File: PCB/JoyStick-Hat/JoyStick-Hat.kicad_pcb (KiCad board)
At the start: 4 copper layers, 65 x 120 mm, 109 parts, among them J1 20021121-00010C4LF, J10 Conn_02x06_Odd_Even, J14 Conn_01x03_Pin, J15 Conn_01x03_Pin, J2 BU2032SM-JJ-GTR, J3 Conn_02x05_Odd_Even, J4 Conn_02x04_Odd_Even, J5 8P8C_LED_Shielded, J6 1757242, J7 Raspberry_Pi_2_3, J8 Conn_02x04_Odd_Even, J9 1755736, M1 D24V22F12, M2 D24V22F5, M3 D24V22F3, SW1 TL3301NF260QG, U1 STM32F446VETx, U4 MAX3535ECWI+T, X1 ABM3B-8.000MHZ-B2-T, X2 ABS07-32.768KHZ-9-T

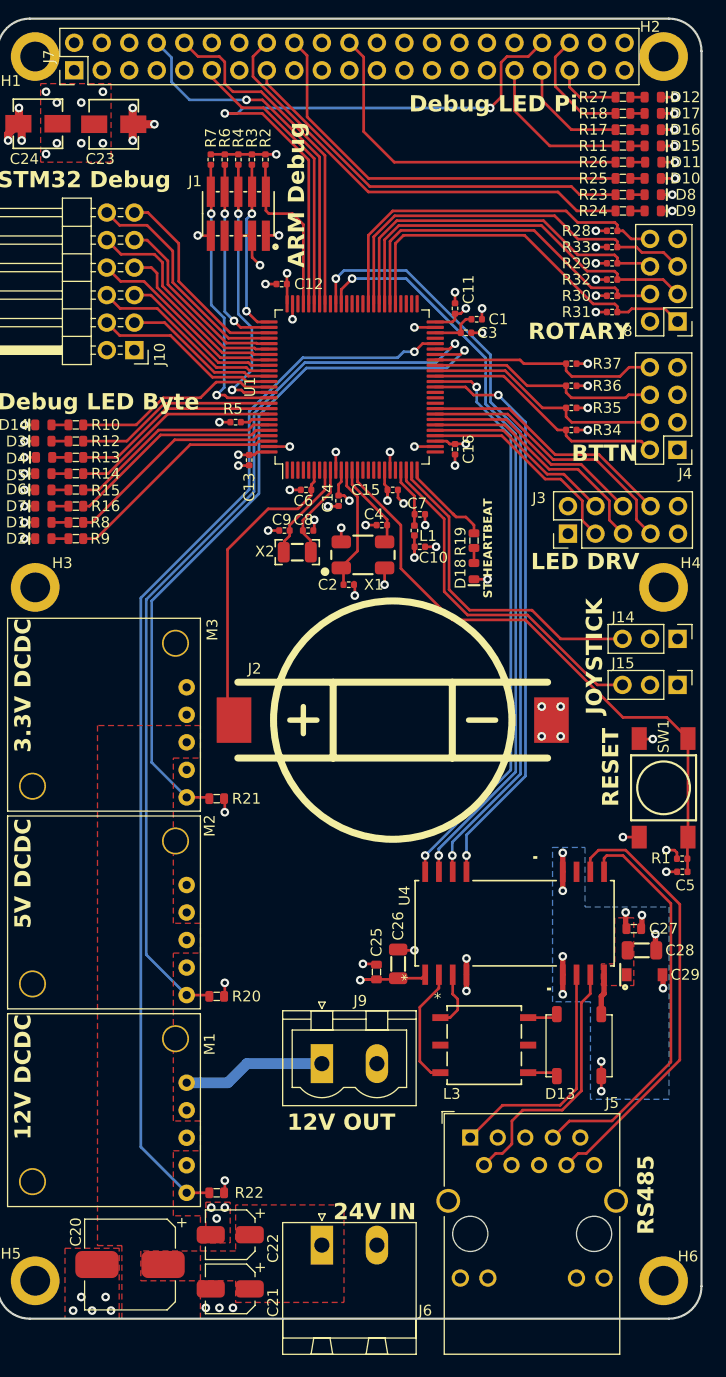
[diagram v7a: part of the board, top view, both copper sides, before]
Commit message: James Fixes and 3D models
Added all the changes that James suggested to the design and then added 3D models to the board for mechanical design purposes. Generated 3D renders of the board and added them to new directory called img.
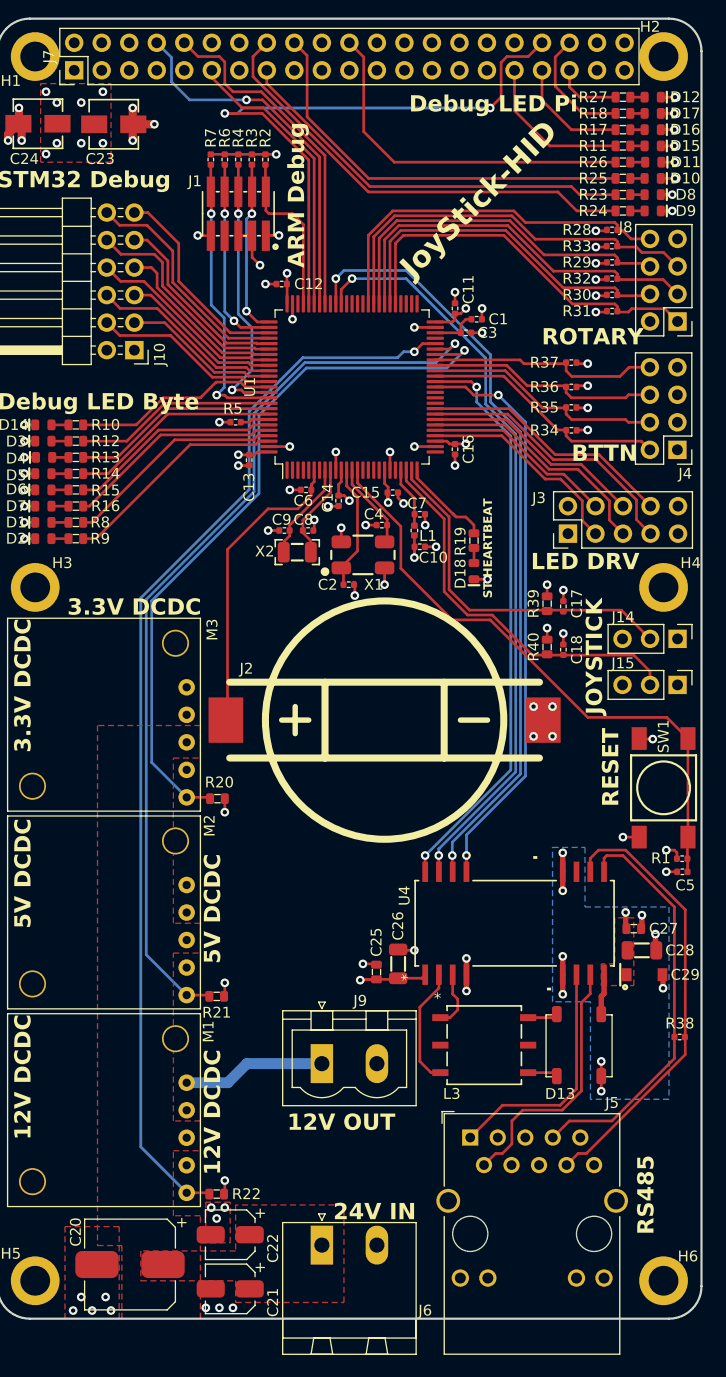
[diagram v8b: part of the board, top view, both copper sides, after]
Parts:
- added C17: C0402C104K9PACTU, AVR-KiCAD-Lib-Resistors:R0402, F.Cu at (252.2, 93.8)
- added C18: C0402C104K9PACTU, AVR-KiCAD-Lib-Resistors:R0402, F.Cu at (252.2, 97.8)
- added R38: AC0402FR-07120RL, AVR-KiCAD-Lib-Resistors:R0402, F.Cu at (263.0, 133.5)
- added R39: RT0603BRD071ML, AVR-KiCAD-Lib-Resistors:R0603, F.Cu at (250.8, 93.5)
- added R40: RT0603BRD071ML, AVR-KiCAD-Lib-Resistors:R0603, F.Cu at (250.8, 97.5)
- R20, R21, R22: value RC0603JR-07270RL -> RC0603FR-072K2L
- R28, R29, R30, R31, R32, R33, R34, R35, R36, R37: value RC0402FR-071KL -> RC0402FR-072K2L
- moved R20 18.3 mm to (220.3, 111.5)
- moved R21 18.2 mm to (220.2, 129.8)
- moved J2 0.75 mm to (235.8, 104.2)
- moved C15 0.25 mm to (236.5, 83.2)
- moved R22 0.12 mm to (220.2, 148.0)
- moved R36 0.11 mm to (253.0, 73.5), turned to 0 degrees
- moved R37 0.10 mm to (253.0, 71.2), turned to 0 degrees
- moved R33 0.09 mm to (256.7, 60.5), turned to 180 degrees
- moved R28 0.09 mm to (256.8, 59.0), turned to 180 degrees
- moved R29 0.09 mm to (256.8, 62.0), turned to 180 degrees
- moved R32 0.09 mm to (256.8, 63.5), turned to 180 degrees
- moved R30 0.08 mm to (256.8, 65.0), turned to 180 degrees
- moved R31 0.08 mm to (256.8, 66.5), turned to 180 degrees
- turned R35 to 0 degrees
- turned R34 to 0 degrees
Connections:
- J14 pad 2: +3.3V -> /JoyStick Interface/JOYSTICK_X
- J14 pad 3: /JoyStick Interface/JOYSTICK_X -> +3.3V
- J15 pad 2: +3.3V -> /JoyStick Interface/JOYSTICK_Y
- J15 pad 3: /JoyStick Interface/JOYSTICK_Y -> +3.3V
- R20 pad 1: /Power/5V_PG -> /Power/3.3V_PG
- R21 pad 1: /Power/3.3V_PG -> /Power/5V_PG
- R28 pad 1: +3.3V -> /JoyStick Interface/ROTARY2_POLE1
- R28 pad 2: /JoyStick Interface/ROTARY2_POLE1 -> +3.3V
- R29 pad 1: +3.3V -> /JoyStick Interface/ROTARY2_POLE2
- R29 pad 2: /JoyStick Interface/ROTARY2_POLE2 -> +3.3V
- R30 pad 1: +3.3V -> /JoyStick Interface/ROTARY2_POLE3
- R30 pad 2: /JoyStick Interface/ROTARY2_POLE3 -> +3.3V
- R31 pad 1: +3.3V -> /JoyStick Interface/ROTARY1_POLE1
- R31 pad 2: /JoyStick Interface/ROTARY1_POLE1 -> +3.3V
- R32 pad 1: +3.3V -> /JoyStick Interface/ROTARY1_POLE2
- R32 pad 2: /JoyStick Interface/ROTARY1_POLE2 -> +3.3V
- R33 pad 1: +3.3V -> /JoyStick Interface/ROTARY1_POLE3
- R33 pad 2: /JoyStick Interface/ROTARY1_POLE3 -> +3.3V
- R34 pad 1: +3.3V -> /JoyStick Interface/BUTTON1
- R34 pad 2: /JoyStick Interface/BUTTON1 -> +3.3V
- R35 pad 1: +3.3V -> /JoyStick Interface/BUTTON2
- R35 pad 2: /JoyStick Interface/BUTTON2 -> +3.3V
- R36 pad 1: +3.3V -> /JoyStick Interface/BUTTON3
- R36 pad 2: /JoyStick Interface/BUTTON3 -> +3.3V
- R37 pad 1: +3.3V -> /JoyStick Interface/BUTTON4
- R37 pad 2: /JoyStick Interface/BUTTON4 -> +3.3V
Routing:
- net /JoyStick Interface/JOYSTICK_Y: track 32.7 -> 36.0 mm
- net /JoyStick Interface/JOYSTICK_X: track 30.4 -> 32.9 mm
- net +3.3V: track 53.9 -> 56.2 mm, vias 24 -> 26
- net GND: track 429.6 -> 431.6 mm, vias 71 -> 73
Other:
- board text added: "Accessibilita Project"
- board text added: "Designed by Adam Vadala-Roth"
- board text added: "JoyStick-HID"
- board text added: "JoyStick-HID Rev 0.1a 2024"
- board text added: "Mobility Independence Foundation"
